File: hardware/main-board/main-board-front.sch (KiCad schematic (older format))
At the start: 19 parts

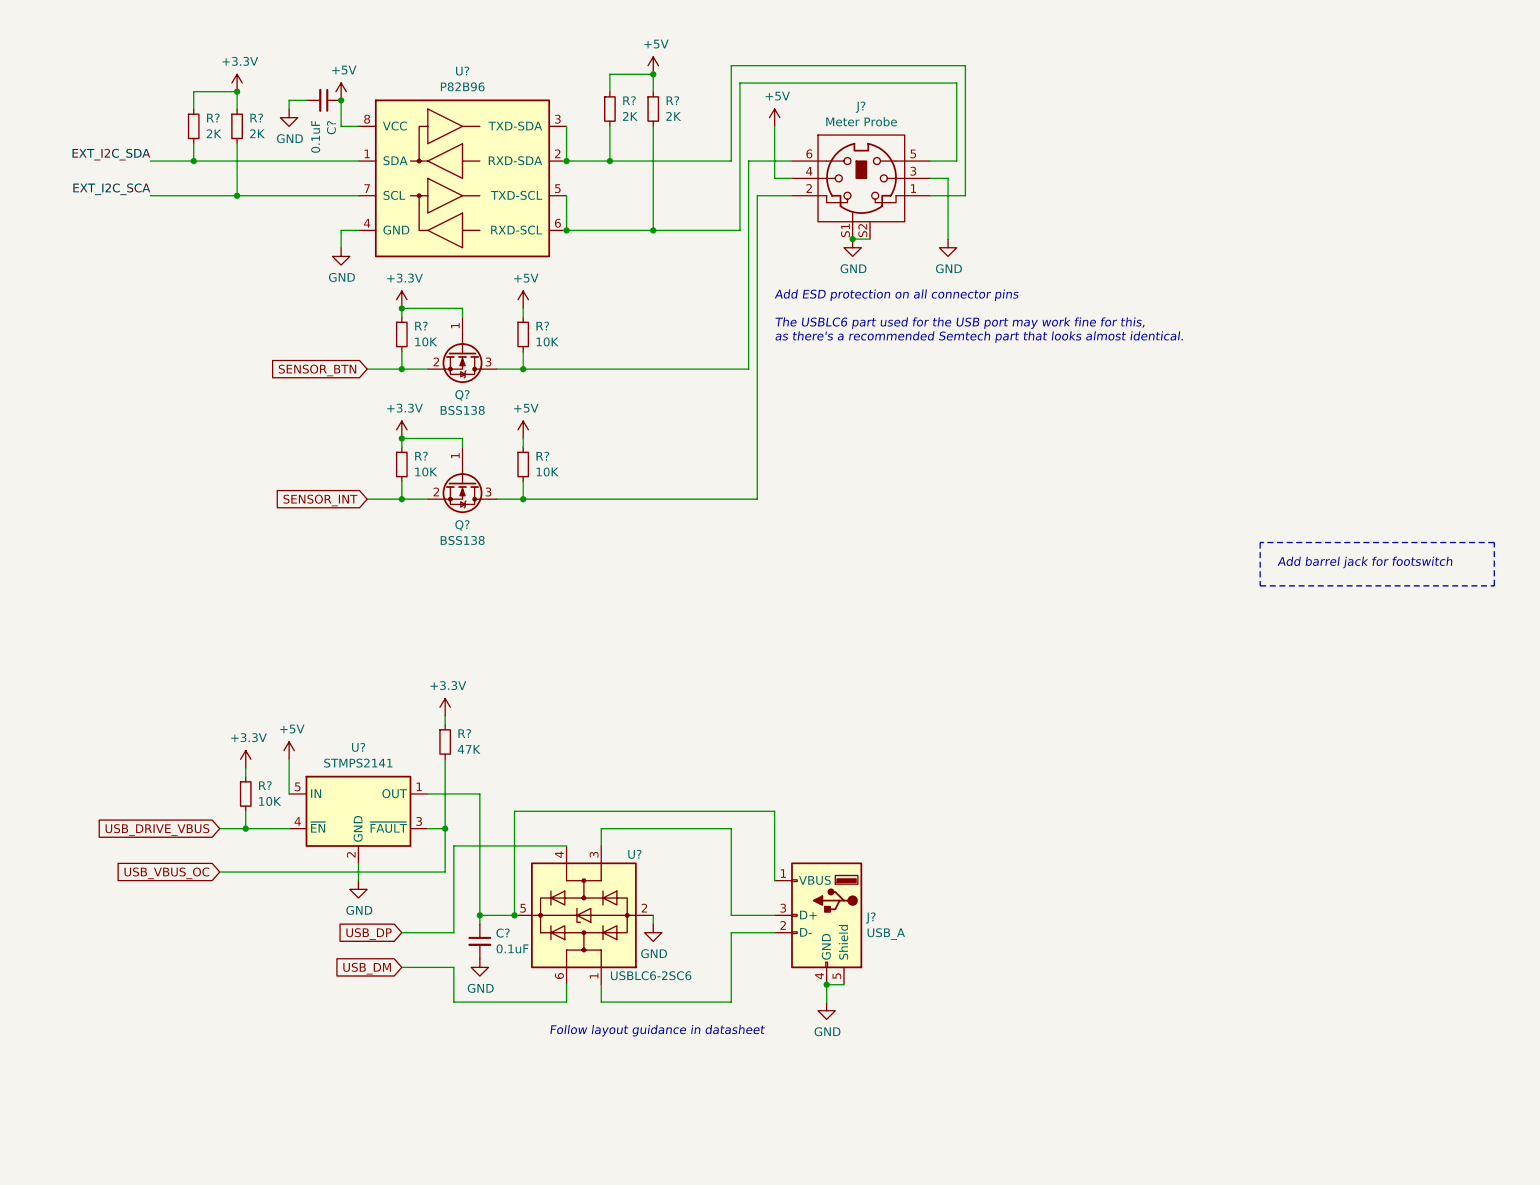
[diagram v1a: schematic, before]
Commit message: More work on main board input and panel connection sheets
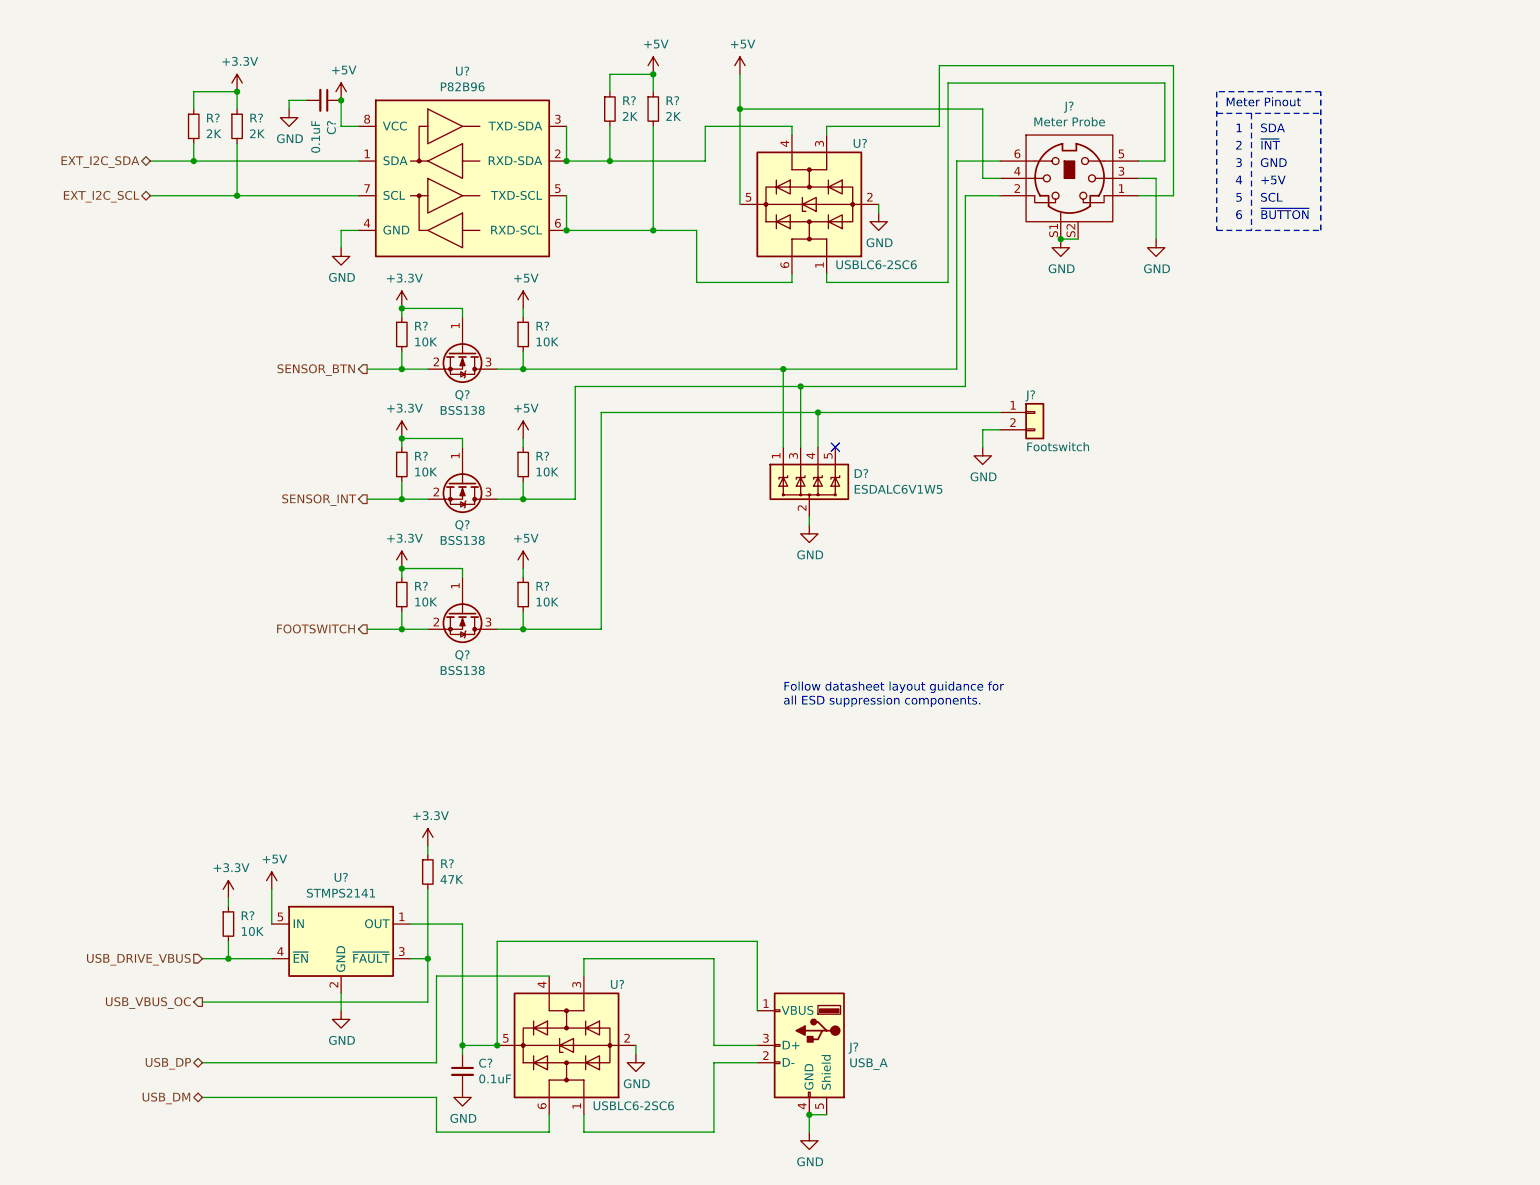
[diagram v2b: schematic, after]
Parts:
- added D?: ESDALC6V1W5, lib_fp:SOT323-5L, symbol Project:ESDALC6V1W5
- added J?: Footswitch, Connector_PinHeader_2.54mm:PinHeader_1x02_P2.54mm_Vertical, symbol Connector_Generic:Conn_01x02
- added Q?: BSS138, Package_TO_SOT_SMD:SOT-23, symbol Transistor_FET:BSS138
- added R? (x2): 10K, symbol Device:R_Small
- added U?: USBLC6-2SC6, Package_TO_SOT_SMD:SOT-23-6, symbol Power_Protection:USBLC6-2SC6
- J?: Description (none) -> CONN RCPT FMALE MINI DIN 6P SLDR; Manufacturer (none) -> CUI Devices; Manufacturer PN (none) -> MD-60SM; Supplier (none) -> Digi-Key; Supplier PN (none) -> CP-2260-ND
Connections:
- net +3V3: now also Q?.1 (G), R?.1
- net +5V: now also R?.1, U?.5 (VBUS)
- net GND: now also D?.2 (GND), J?.2 (Pin_2), U?.2 (GND)
- net at R?.2, U?.2 (RXD-SDA), U?.3 (TXD-SDA): now also U?.4 (I/O2); no longer J?.1
- net at R?.2, U?.5 (TXD-SCL), U?.6 (RXD-SCL): now also U?.6 (I/O1); no longer J?.5
- net at J?.2, Q?.3 (D), R?.2: now also D?.3 (IO2)
- net at J?.6, Q?.3 (D), R?.2: now also D?.1 (IO1)
- net EXT_I2C_SCA renamed EXT_I2C_SCL
- new net: D?.4 (IO3), J?.1 (Pin_1), Q?.3 (D), R?.2
- new net: J?.5, U?.1 (I/O1)
- new net: J?.1, U?.3 (I/O2)
- new net FOOTSWITCH: Q?.2 (S), R?.2
- no-connect marks 0 -> 1
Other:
- note added: "+5V"
- note added: "1"
- note added: "2"
- note added: "3"
- note added: "4"
- note added: "5"
- note added: "6"
- note added: "Follow datasheet layout guidance for\nall ESD suppression components."
- note added: "GND"
- note added: "Meter Pinout"
- note added: "SCL"
- note added: "SDA"
- note added: "~BUTTON"
- note added: "~INT"
- note removed: "Add ESD protection on all connector pins\n\nThe USBLC6 part used for the USB port may work fine for this,\nas there's a recommended Semtech part that looks almost identical."
- note removed: "Add barrel jack for footswitch"
- note removed: "Follow layout guidance in datasheet"
- moved on the sheet: C?, J?, R?, U?
